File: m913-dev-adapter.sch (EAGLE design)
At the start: 23 parts, among them U1 SCREW-M2X8, U10 FX2-20S-1.27DS, U2 SCREW-M2X8, U3 NUT-M2-SELFLOCK, U4 NUT-M2-SELFLOCK, U5 FX2-20P-1.27DS, U6 SCREW-M2X8, U7 SCREW-M2X8, U8 NUT-M2-SELFLOCK, U9 NUT-M2-SELFLOCK

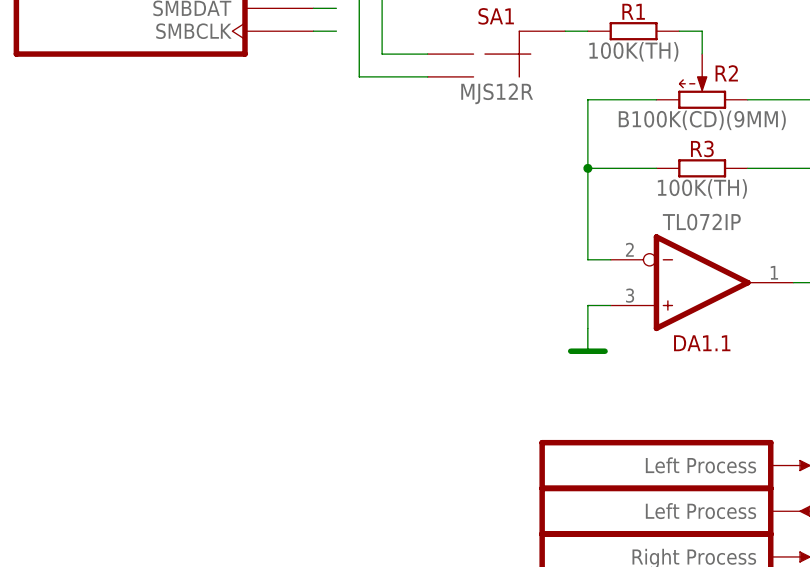
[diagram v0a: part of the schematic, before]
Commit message: Add CV knob
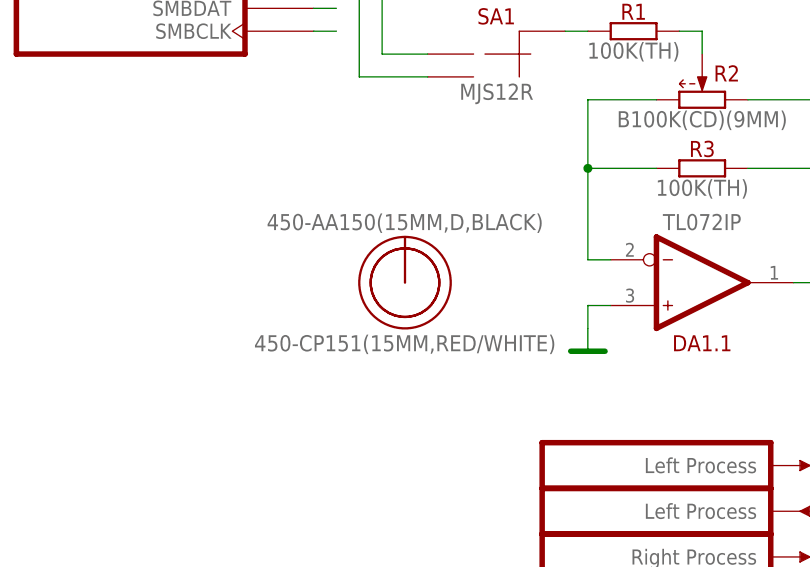
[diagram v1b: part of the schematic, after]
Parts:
- added O1: 450-AA150(15MM,D,BLACK), hardware:450-AA150(15MM,D,BLACK)
- added O2: 450-CP151(15MM,RED/WHITE), hardware:450-CP151(15MM,RED/WHITE)
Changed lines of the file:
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@@
 <part name="PWR2" library="supply" deviceset="-15V" device=""/>
 <part name="GND3" library="supply" deviceset="GND" device=""/>
+<part name="O1" library="hardware" deviceset="450-AA?" device="150(15MM,D,BLACK)"/>
+<part name="O2" library="hardware" deviceset="450-C?" device="P151(15MM,RED/WHITE)"/>
 </parts>
 <sheets>
@@
 <instance part="PWR2" gate="G$1" x="121.92" y="-109.22" rot="R90"/>
 <instance part="GND3" gate="VR1" x="134.62" y="-132.08"/>
+<instance part="O1" gate="G$1" x="43.18" y="-88.9"/>
+<instance part="O2" gate="G$1" x="43.18" y="-88.9"/>
 </instances>
 <busses>
